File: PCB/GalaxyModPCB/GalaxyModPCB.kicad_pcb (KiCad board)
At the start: 2 copper layers, 63.5 x 38.2 mm, 57 parts, among them J1 LED RGBW Connector, J2 USB to UART, J3 Motor Connector, J4 Projector Connector, J6 Power Header, J7 Boot mode, Q1 IRLML0030, Q2 IRLML0030, Q3 IRLML0030, Q4 IRLML0030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

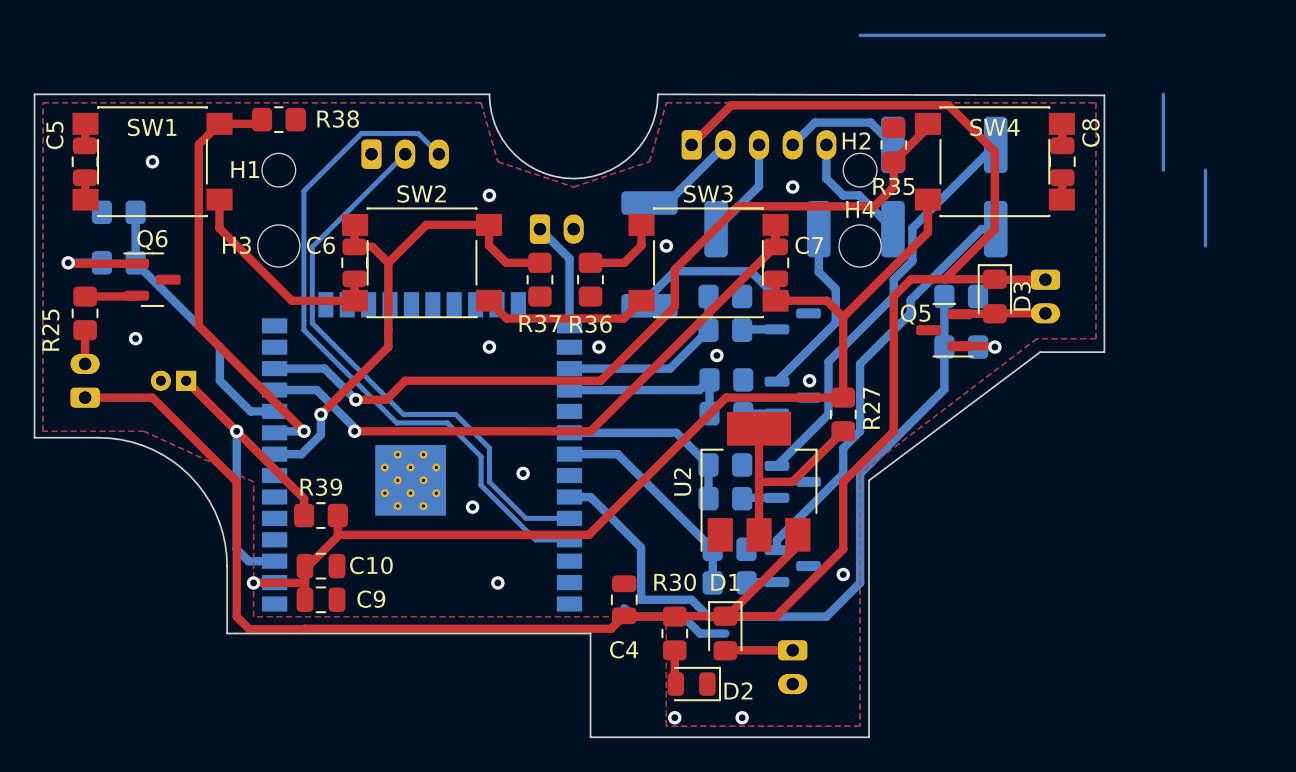
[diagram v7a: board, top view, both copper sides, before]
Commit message: Removed old traces
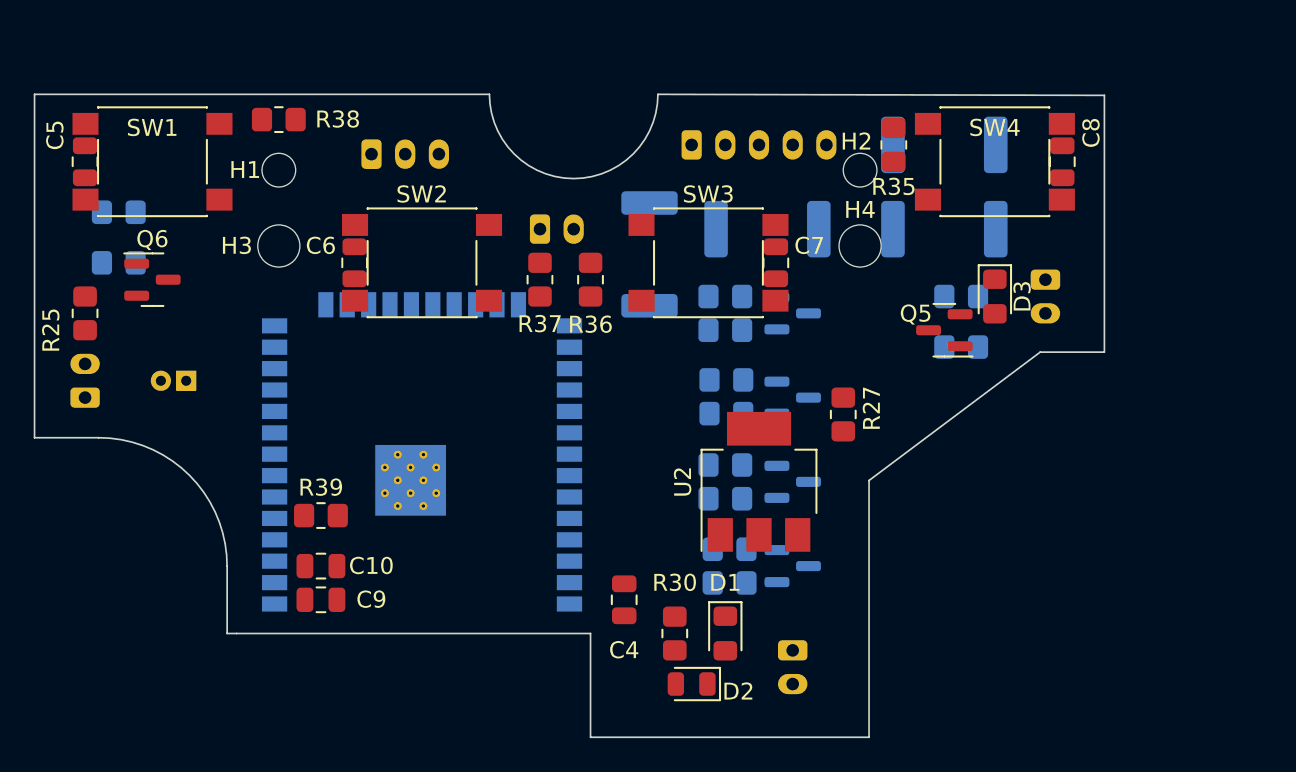
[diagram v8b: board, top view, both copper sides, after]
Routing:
- net Net-(C4-Pad1): track 117.8 -> 0.00 mm
- net Net-(C10-Pad1): track 90.5 -> 0.00 mm, vias 1 -> 0
- net Net-(C8-Pad1): track 50.3 -> 0.00 mm, vias 1 -> 0
- net Net-(C7-Pad1): track 42.7 -> 0.00 mm, vias 1 -> 0
- net Net-(R33-Pad2): track 41.9 -> 0.00 mm
- net Net-(J2-Pad3): track 40.1 -> 0.00 mm
- net Net-(J2-Pad2): track 33.6 -> 0.00 mm
- net Net-(C6-Pad1): track 30.4 -> 0.00 mm, vias 1 -> 0
- net Net-(C5-Pad1): track 27.1 -> 0.00 mm, vias 1 -> 0
- net Net-(Q4-Pad2): track 24.9 -> 0.00 mm
- net Net-(Q3-Pad2): track 24.4 -> 0.00 mm
- net Net-(C2-Pad1): track 20.4 -> 0.00 mm, vias 1 -> 0
- net Net-(R31-Pad2): track 16.3 -> 0.00 mm
- net Net-(R20-Pad1): track 12.8 -> 0.00 mm
- net Net-(R27-Pad1): track 12.5 -> 0.00 mm
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- removed copper zone on B.Cu, net GNDREF
- removed copper zone on F.Cu, net GNDREF
